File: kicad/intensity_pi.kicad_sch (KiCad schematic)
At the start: 63 parts, among them J1 Input A, J2 Input B / Setpoint, J3 Monitor, J4 Output, J7 select 1, SW5 SW_DPDT_x2, SW6 SW_SP4T, U1 LM4040DBZ-5, U10 OPA189, U11 PC817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

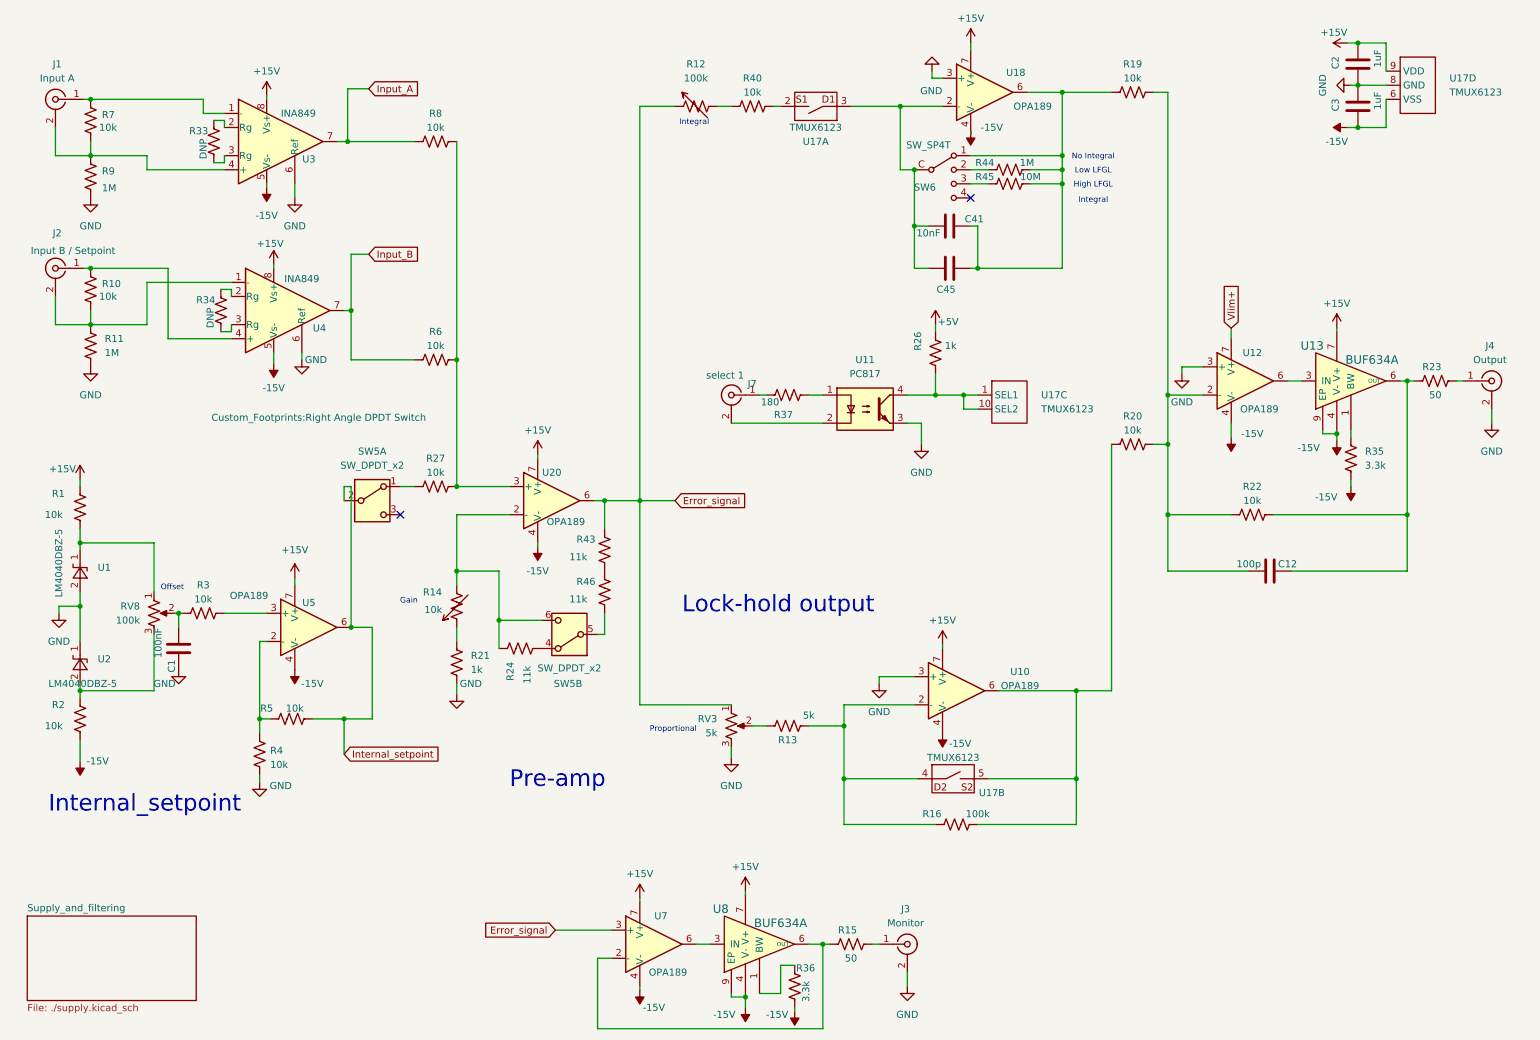
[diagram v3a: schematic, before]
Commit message: Added all features to schematic, TODO: fix pot footprint and layout pcb
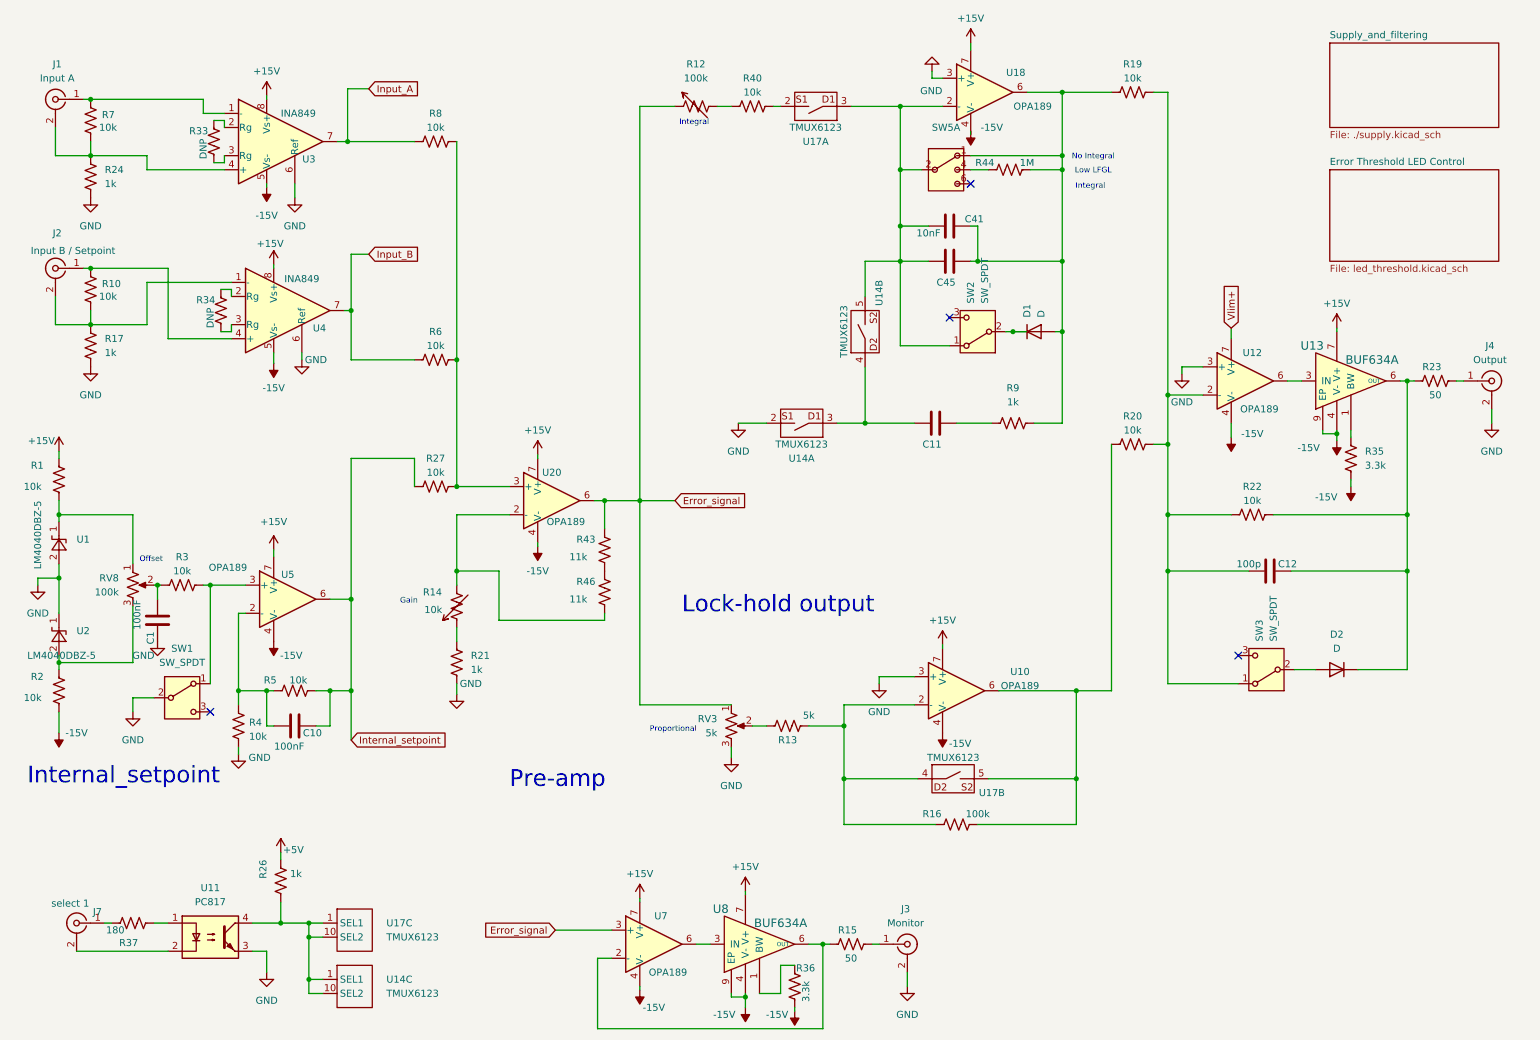
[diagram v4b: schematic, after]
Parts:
- removed C2, C3: 1uF, Capacitor_SMD:C_0805_2012Metric, symbol Device:C
- removed R11: 1M, Resistor_SMD:R_0805_2012Metric, symbol Device:R_US
- removed R45: 10M, Resistor_SMD:R_0805_2012Metric, symbol Device:R_US
- removed SW5: SW_DPDT_x2, Custom_Footprints:Right Angle DPDT Switch, symbol Switch:SW_DPDT_x2
- removed SW6: SW_SP4T, lib:SLB1470, symbol local_lib:SW_SP4T
- removed unit 4 of U17
- added C10: 100nF, Capacitor_SMD:C_0805_2012Metric, symbol Device:C
- added C11: C, Capacitor_THT:C_Axial_L3.8mm_D2.6mm_P7.50mm_Horizontal, symbol Device:C
- added D1, D2: D, Package_TO_SOT_SMD:TSOT-23, symbol Device:D
- added R17: 1k, Resistor_SMD:R_0805_2012Metric, symbol Device:R_US
- added SW1: SW_SPDT, Custom_Footprints:Right Angle SPDT Switch, symbol Switch:SW_SPDT
- added SW2, SW3: SW_SPDT, Custom_Footprints:TDD DIP Switch, symbol Switch:SW_SPDT
- added SW5: ~, Custom_Footprints:Right Angle 3PDT Switch, symbol Custom_Symbols:DP3T_1
- added U14: TMUX6123, Package_SO:VSSOP-10_3x3mm_P0.5mm, symbol library_intensity_pi:TMUX6123_split
- R24: value 11k -> 1k
- R9: value 1M -> 1k; DIGIKEY 2019-RN73H2ATTD1002B25CT-ND -> (none)
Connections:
- net GND: now also R24.1, R17.1, SW1.2 (B), U14.2; no longer R9.1
- net Internal_setpoint: now also R27.1, C10.1
- net at J1.2 (Ext), R7.1, U3.4 (+): now also R24.2; no longer R9.2
- net at R4.2, R5.1, U5.2 (-): now also C10.2
- net at R3.2, U5.3 (+): now also SW1.1 (A)
- net at C12.2, R19.2, R20.2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: now also SW3.1 (A)
- net at C12.1, R22.2, R23.1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: now also D2.1 (K)
- net at J2.2 (Ext), R10.1, U4.1 (-): now also R17.2
- net at C41.1, C45.2, R19.1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: now also R9.1, D1.2 (A), SW5.1
- net at C41.2, C45.1, U17.3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: now also SW2.1 (A), SW5.2, U14.5
- net at R14.2, U20.2 (-): now also R46.1; no longer R24.2
- net at R26.2, U11.4, U17.1 (SEL1)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: now also U14.1 (SEL1), U14.10 (SEL2)
- net at R44.1: now also SW5.4
- new net: D1.1 (K), SW2.2 (B)
- new net: C11.2, R9.2
- new net: D2.2 (A), SW3.2 (B)
- new net: C11.1, U14.3, U14.4
- no-connect marks 2 -> 4
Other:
- added sheet Error Threshold LED Control (led_threshold.kicad_sch)
- note removed: "High LFGL"
- moved on the sheet: C1, C45, J7, R1, R2, R26, R3, R37, R4, R5, RV8, U1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

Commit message: Finished Schematic and Assigning Footprint pending Review, TODO: Layout Board
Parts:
- R12, R14, RV3, RV8: footprint Connector_PinHeader_2.54mm:PinHeader_1x03_P2.54mm_Vertical -> Custom_Footprints:Bourns Circular Pots
- SW5: DIGIKEY (none) -> EG6100-ND; PARTNO (none) -> 1004P6T1B4M7RE
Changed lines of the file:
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@@
 			)
 		)
-		(property "Footprint" "Connector_PinHeader_2.54mm:PinHeader_1x03_P2.54mm_Vertical"
+		(property "Footprint" "Custom_Footprints:Bourns Circular Pots"
 			(at 140.97 142.24 0)
 			(effects
@@
 			)
 		)
-		(property "Footprint" "Connector_PinHeader_2.54mm:PinHeader_1x03_P2.54mm_Vertical"
+		(property "Footprint" "Custom_Footprints:Bourns Circular Pots"
 			(at 93.218 120.65 90)
 			(effects
@@
 			)
 		)
+		(property "DIGIKEY" "EG6100-ND"
+			(at 179.07 41.91 0)
+			(effects
+				(font
+					(size 1.27 1.27)
+				)
+				(hide yes)
+			)
+		)
+		(property "PARTNO" "1004P6T1B4M7RE"
+			(at 179.07 41.91 0)
+			(effects
+				(font
+					(size 1.27 1.27)
+				)
+				(hide yes)
+			)
+		)
 		(pin "9"
 		)
@@
 			)
 		)
-		(property "Footprint" "Connector_PinHeader_2.54mm:PinHeader_1x03_P2.54mm_Vertical"
+		(property "Footprint" "Custom_Footprints:Bourns Circular Pots"
 			(at 33.02 116.84 0)
 			(effects
@@
 			)
 		)
-		(property "Footprint" "Connector_PinHeader_2.54mm:PinHeader_1x03_P2.54mm_Vertical"
+		(property "Footprint" "Custom_Footprints:Bourns Circular Pots"
 			(at 134.62 32.258 90)
 			(effects

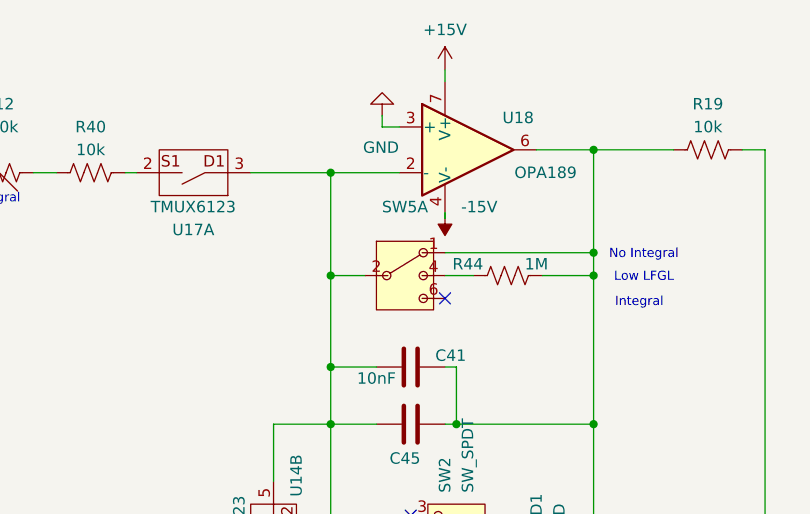
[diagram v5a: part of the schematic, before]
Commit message: Fixed LED Threshold schematic, added second power input screw terminal, first attempt at final placement and routing
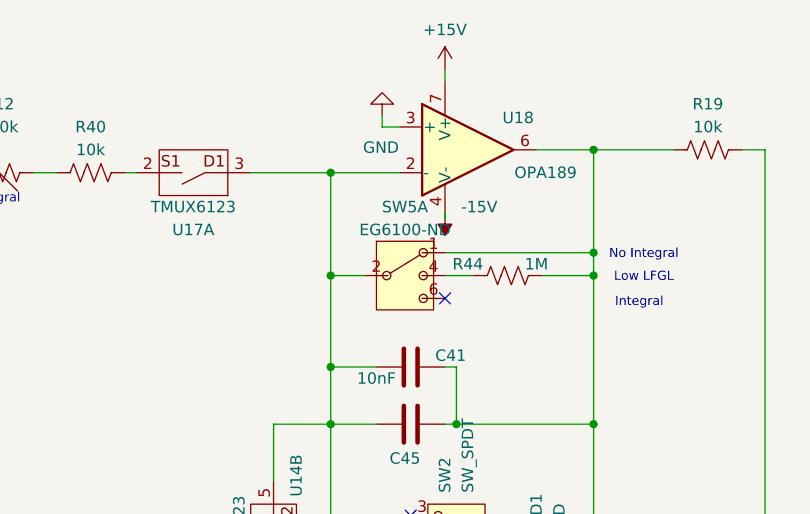
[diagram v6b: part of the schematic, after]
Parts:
- J1, J2, J3, J4, J7: DIGIKEY (none) -> ARF1065-ND; PARTNO (none) -> 31-5431
- R1, R14, R2: DIGIKEY (none) -> 2019-RN73H2ATTD1002B25CT-ND
- SW5: value ~ -> EG6100-ND
- U11: DIGIKEY (none) -> ISP817A; PARTNO (none) -> ISP817A

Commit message: Final Schematic, Reworking PCB pt 1
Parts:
- C11: footprint Capacitor_THT:C_Axial_L3.8mm_D2.6mm_P7.50mm_Horizontal -> Capacitor_SMD:C_0805_2012Metric
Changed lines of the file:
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@@
 			)
 		)
-		(property "Footprint" "Capacitor_THT:C_Axial_L3.8mm_D2.6mm_P7.50mm_Horizontal"
+		(property "Footprint" "Capacitor_SMD:C_0805_2012Metric"
 			(at 181.61 86.6648 0)
 			(effects

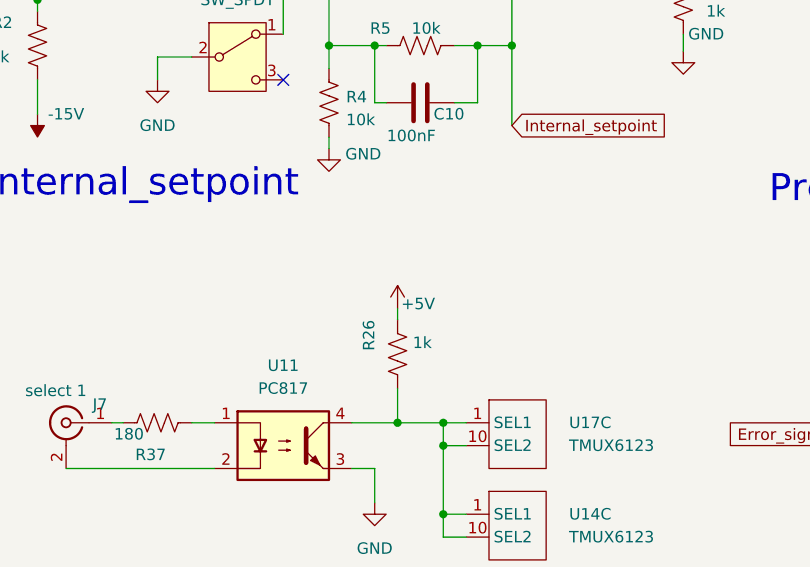
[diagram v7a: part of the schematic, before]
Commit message: Condensed Layout, Removed 5V supply, Shortened Board
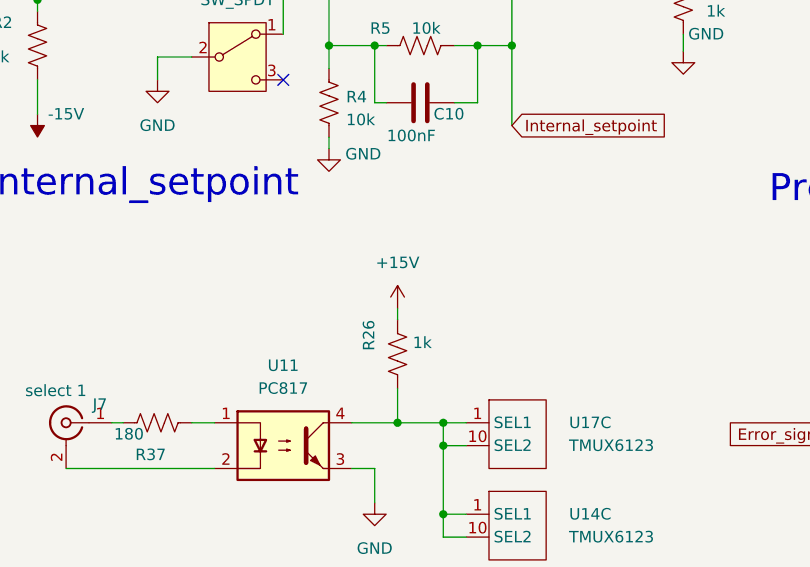
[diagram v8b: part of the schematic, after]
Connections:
- net +5V is gone; now on net +15V: R26.1
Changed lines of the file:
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@@
-	)
-	(symbol
-		(lib_id "power:+5V")
-		(at 59.69 165.1 0)
-		(unit 1)
-		(exclude_from_sim no)
-		(in_bom yes)
-		(on_board yes)
-		(dnp no)
-		(property "Reference" "#PWR082"
-			(at 59.69 168.91 0)
-			(effects
-				(font
-					(size 1.27 1.27)
-				)
-				(hide yes)
-			)
-		)
-		(property "Value" "+5V"
-			(at 61.976 164.592 0)
-			(effects
-				(font
-					(size 1.27 1.27)
-				)
-			)
-		)
-		(property "Footprint" ""
-			(at 59.69 165.1 0)
-			(effects
-				(font
-					(size 1.27 1.27)
-				)
-				(hide yes)
-			)
-		)
-		(property "Datasheet" ""
-			(at 59.69 165.1 0)
-			(effects
-				(font
-					(size 1.27 1.27)
-				)
-				(hide yes)
-			)
-		)
-		(property "Description" "Power symbol creates a global label with name \"+5V\""
-			(at 59.69 165.1 0)
-			(effects
-				(font
-					(size 1.27 1.27)
-				)
-				(hide yes)
-			)
-		)
-		(pin "1"
-		)
-		(instances
-			(project "intensity_pi"
-				(path "/3a3d7bcb-6fa5-41ef-9ea1-6d4ab7c492fd"
-					(reference "#PWR082")
-					(unit 1)
-				)
-			)
-		)
 	)
 	(symbol
@@
 					(unit 1)
 				)
+			)
+		)
+	)
+	(symbol
+		(lib_id "power:+15V")
+		(at 59.69 165.1 0)
+		(unit 1)
+		(exclude_from_sim no)
+		(in_bom yes)
+		(on_board yes)
+		(dnp no)
+		(fields_autoplaced yes)
+		(property "Reference" "#PWR082"
+			(at 59.69 168.91 0)
+			(effects
+				(font
+					(size 1.27 1.27)
+				)
+				(hide yes)
+			)
+		)
+		(property "Value" "+15V"
+			(at 59.69 160.02 0)
+			(effects
+				(font
+					(size 1.27 1.27)
+				)
+			)
+		)
+		(property "Footprint" ""
+			(at 59.69 165.1 0)
+			(effects
+				(font
+					(size 1.27 1.27)
+				)
+				(hide yes)
+			)
+		)
+		(property "Datasheet" ""
+			(at 59.69 165.1 0)
+			(effects
+				(font
+					(size 1.27 1.27)
+				)
+				(hide yes)
+			)
+		)
+		(property "Description" "Power symbol creates a global label with name \"+15V\""
+			(at 59.69 165.1 0)
+			(effects
+				(font
+					(size 1.27 1.27)
+				)
+				(hide yes)
+			)
+		)
+		(pin "1"
+		)
+		(instances
+			(project ""
+				(path "/3a3d7bcb-6fa5-41ef-9ea1-6d4ab7c492fd"
+					(reference "#PWR082")
+					(unit 1)
+				)
